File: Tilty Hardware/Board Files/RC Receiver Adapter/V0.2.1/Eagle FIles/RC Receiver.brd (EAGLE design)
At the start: 38.1 x 50.8 mm, 32 parts, among them U1 ATMEGA328P, U2 LM2931, U3 AP7313SOT23R, U4 PCA9306, Y1 16MHz

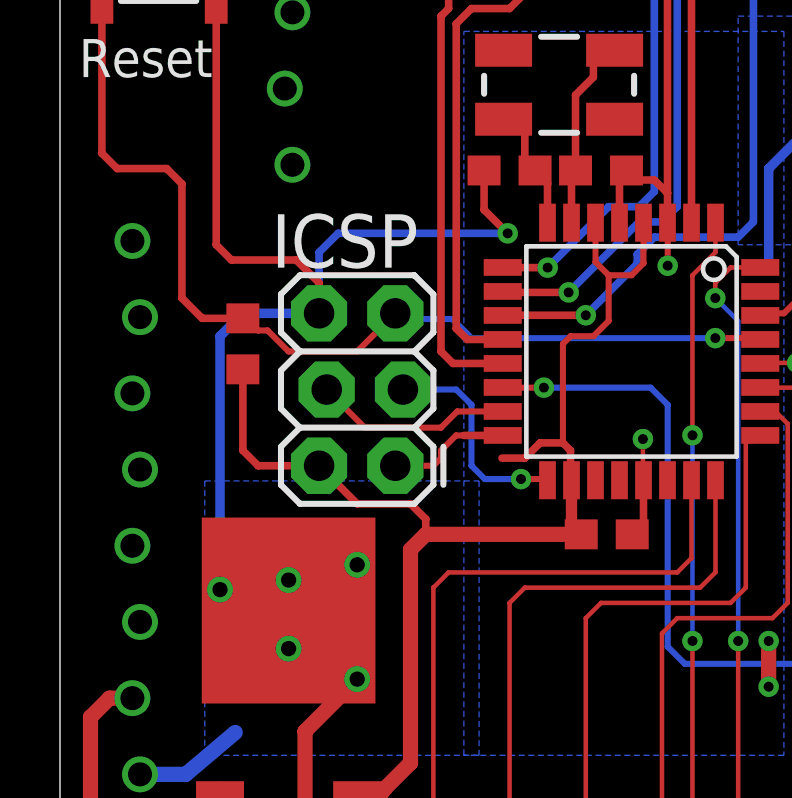
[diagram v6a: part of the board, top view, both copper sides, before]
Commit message: Moved reset pull-up to straighten traces
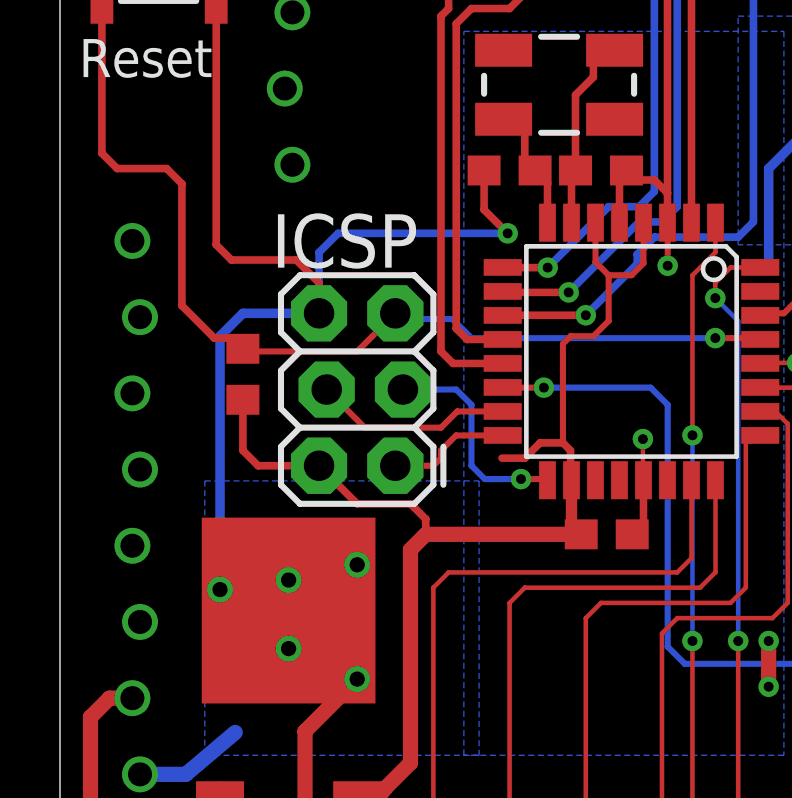
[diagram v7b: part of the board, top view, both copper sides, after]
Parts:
- moved R1 1.02 mm to (6.10, 24.6)
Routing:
- net +5V: track 170.1 -> 168.9 mm
- net GND: track 194.5 -> 195.5 mm
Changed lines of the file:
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@@
 </element>
 <element name="C3" library="resistor" package="C0603" value="0.1uF" x="18.2245" y="19.304" smashed="yes"/>
-<element name="R1" library="resistor" package="R0603" value="10k" x="6.096" y="25.654" smashed="yes" rot="R90"/>
+<element name="R1" library="resistor" package="R0603" value="10k" x="6.096" y="24.638" smashed="yes" rot="R90"/>
 <element name="R2" library="resistor" package="R0603" value="" x="26.162" y="22.733" smashed="yes" rot="R270">
 <attribute name="VALUE" x="24.13" y="23.622" size="1.27" layer="27" rot="R270"/>
@@
 <via x="23.622" y="14.224" extent="1-16" drill="0.3302"/>
 <via x="23.622" y="15.748" extent="1-16" drill="0.3302"/>
-<wire x1="7.62" y1="16.764" x2="7.62" y2="17.78" width="0" layer="19" extent="1-1"/>
-<wire x1="18.65" y1="29.6926" x2="14.9225" y2="29.337" width="0" layer="19" extent="1-1"/>
 <wire x1="23.622" y1="14.224" x2="23.622" y2="15.748" width="0.508" layer="1"/>
+<wire x1="7.62" y1="16.764" x2="7.62" y2="17.78" width="0.508" layer="1"/>
 </signal>
 <signal name="+24V">
@@
 <wire x1="20.574" y1="46.863" x2="23.114" y2="46.863" width="0.3175" layer="16"/>
 <wire x1="23.114" y1="46.863" x2="25.654" y2="46.863" width="0.3175" layer="16"/>
-<wire x1="6.262" y1="24.638" x2="6.096" y2="24.804" width="0.2032" layer="1"/>
 <wire x1="15.494" y1="21.844" x2="16.002" y2="22.352" width="0.254" layer="1"/>
 <wire x1="16.002" y1="22.352" x2="16.764" y2="22.352" width="0.254" layer="1"/>
@@
 <wire x1="10.16" y1="6.946" x2="10.121" y2="6.985" width="0.508" layer="1"/>
 <wire x1="15.494" y1="21.844" x2="14.732" y2="21.844" width="0.254" layer="1"/>
-<wire x1="6.096" y1="22.098" x2="6.096" y2="24.804" width="0.254" layer="1"/>
+<wire x1="6.096" y1="22.098" x2="6.096" y2="23.788" width="0.254" layer="1"/>
 <contactref element="R5" pad="2"/>
 <contactref element="U4" pad="P$8"/>
@@
 <contactref element="U1" pad="16"/>
 <contactref element="JP6" pad="1"/>
-<wire x1="14.7574" y1="22.6" x2="13.456" y2="22.6" width="0.254" layer="1"/>
-<wire x1="13.456" y1="22.6" x2="13.202" y2="22.6" width="0.2032" layer="1"/>
 <wire x1="13.202" y1="22.6" x2="12.7" y2="22.098" width="0.2032" layer="1"/>
 <wire x1="12.7" y1="22.098" x2="12.7" y2="21.844" width="0.2032" layer="1"/>
 <wire x1="12.7" y1="21.844" x2="12.446" y2="21.59" width="0.2032" layer="1"/>
 <wire x1="12.446" y1="21.59" x2="11.176" y2="21.59" width="0.2032" layer="1"/>
+<wire x1="13.202" y1="22.6" x2="14.7574" y2="22.6" width="0.2032" layer="1"/>
 </signal>
 <signal name="SCK">
@@
 <contactref element="U1" pad="29"/>
 <via x="21.844" y="25.8445" extent="1-16" drill="0.3302"/>
-<wire x1="6.184" y1="26.416" x2="6.096" y2="26.504" width="0.2032" layer="1"/>
 <wire x1="21.844" y1="25.8445" x2="13.716" y2="25.8445" width="0.2032" layer="16"/>
-<wire x1="6.096" y1="26.504" x2="4.738" y2="26.504" width="0.254" layer="1"/>
-<wire x1="4.738" y1="26.504" x2="4.064" y2="27.178" width="0.254" layer="1"/>
 <contactref element="S1" pad="1"/>
-<wire x1="4.064" y1="27.178" x2="4.064" y2="30.988" width="0.254" layer="1"/>
+<wire x1="4.064" y1="26.924" x2="4.064" y2="30.988" width="0.254" layer="1"/>
 <wire x1="4.064" y1="30.988" x2="3.556" y2="31.496" width="0.254" layer="1"/>
 <wire x1="3.556" y1="31.496" x2="1.905" y2="31.496" width="0.254" layer="1"/>
@@
 <wire x1="21.844" y1="25.8445" x2="23.2981" y2="25.8445" width="0.2032" layer="1"/>
 <wire x1="23.2981" y1="25.8445" x2="23.3426" y2="25.8" width="0.2032" layer="1"/>
-<wire x1="6.184" y1="26.416" x2="6.2865" y2="26.416" width="0.2032" layer="1"/>
-<wire x1="6.2865" y1="26.416" x2="6.604" y2="26.0985" width="0.2032" layer="1"/>
-<wire x1="6.604" y1="26.0985" x2="6.9215" y2="26.0985" width="0.2032" layer="1"/>
-<wire x1="6.9215" y1="26.0985" x2="7.62" y2="25.4" width="0.2032" layer="1"/>
-<wire x1="7.62" y1="25.4" x2="9.906" y2="25.4" width="0.2032" layer="1"/>
 <wire x1="9.906" y1="25.4" x2="11.176" y2="26.67" width="0.2032" layer="1"/>
 <wire x1="13.716" y1="25.8445" x2="13.081" y2="26.4795" width="0.2032" layer="16"/>
 <wire x1="13.081" y1="26.4795" x2="11.3665" y2="26.4795" width="0.2032" layer="16"/>
 <wire x1="11.3665" y1="26.4795" x2="11.176" y2="26.67" width="0.2032" layer="16"/>
+<wire x1="9.906" y1="25.4" x2="6.184" y2="25.4" width="0.2032" layer="1"/>
+<wire x1="6.184" y1="25.4" x2="6.096" y2="25.488" width="0.2032" layer="1"/>
+<wire x1="4.064" y1="26.924" x2="5.1435" y2="25.8445" width="0.254" layer="1"/>
+<wire x1="5.1435" y1="25.8445" x2="5.7395" y2="25.8445" width="0.254" layer="1"/>
+<wire x1="5.7395" y1="25.8445" x2="6.096" y2="25.488" width="0.254" layer="1"/>
 </signal>
 <signal name="RC_IN1">

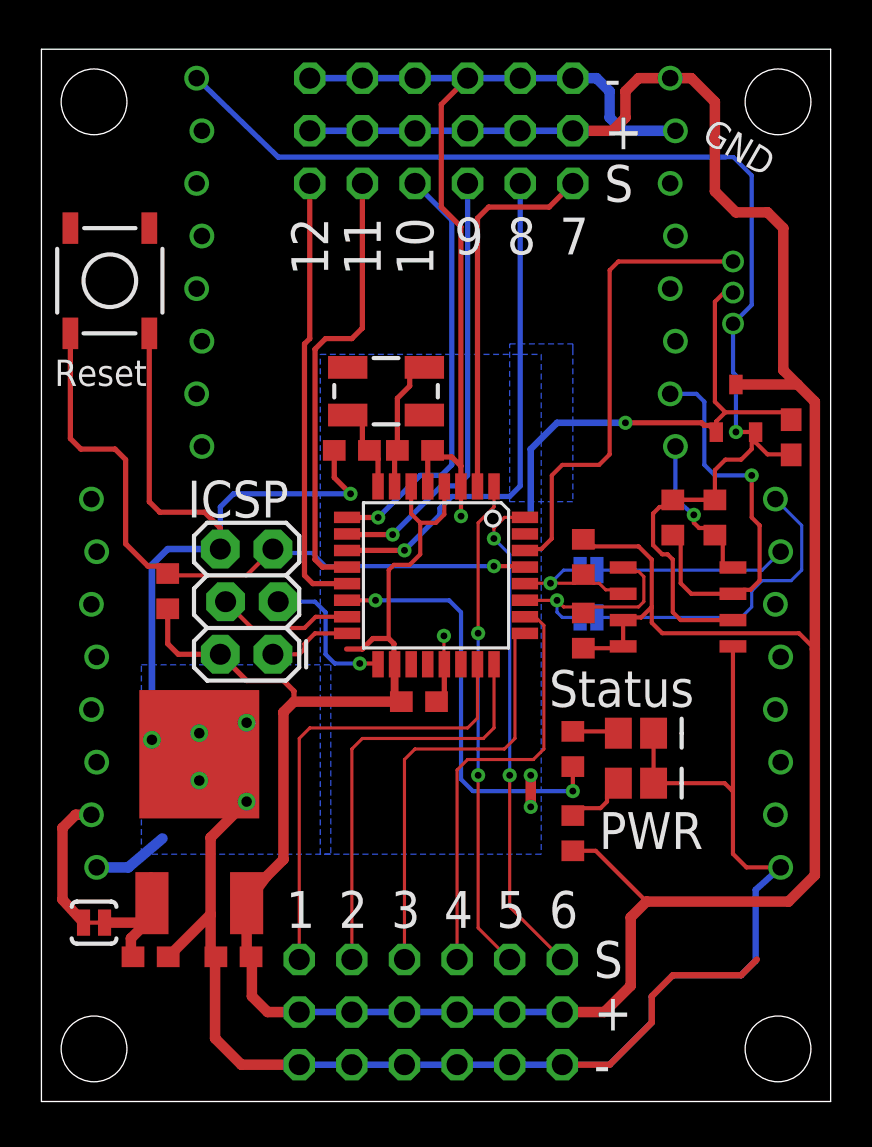
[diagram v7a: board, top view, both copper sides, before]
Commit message: Narrowed all I/O traces to be uniform width
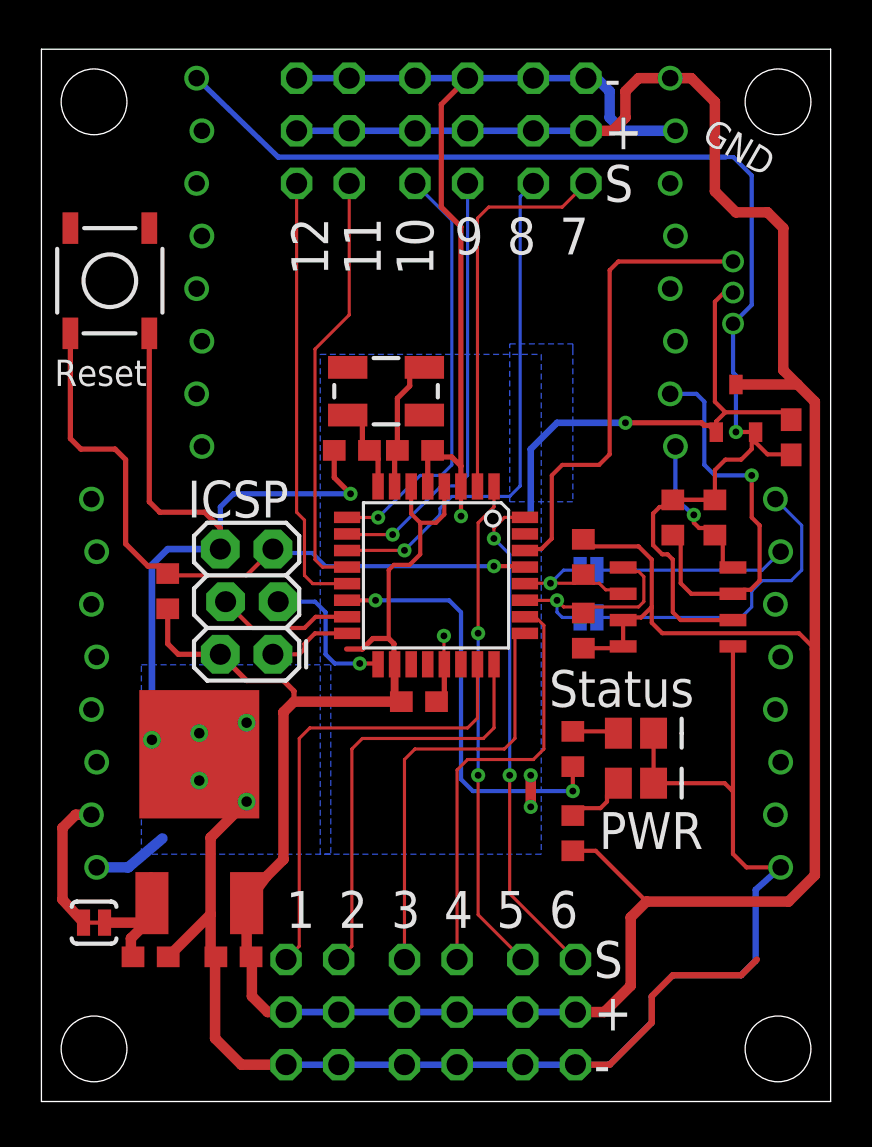
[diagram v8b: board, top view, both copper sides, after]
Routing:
- net SERVO_2: track 21.6 -> 20.5 mm
- net SERVO_6: track 18.2 -> 18.9 mm
- net +5V: track 168.9 -> 169.5 mm
